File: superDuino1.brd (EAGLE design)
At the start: 70.8 x 71.1 mm, 25 parts

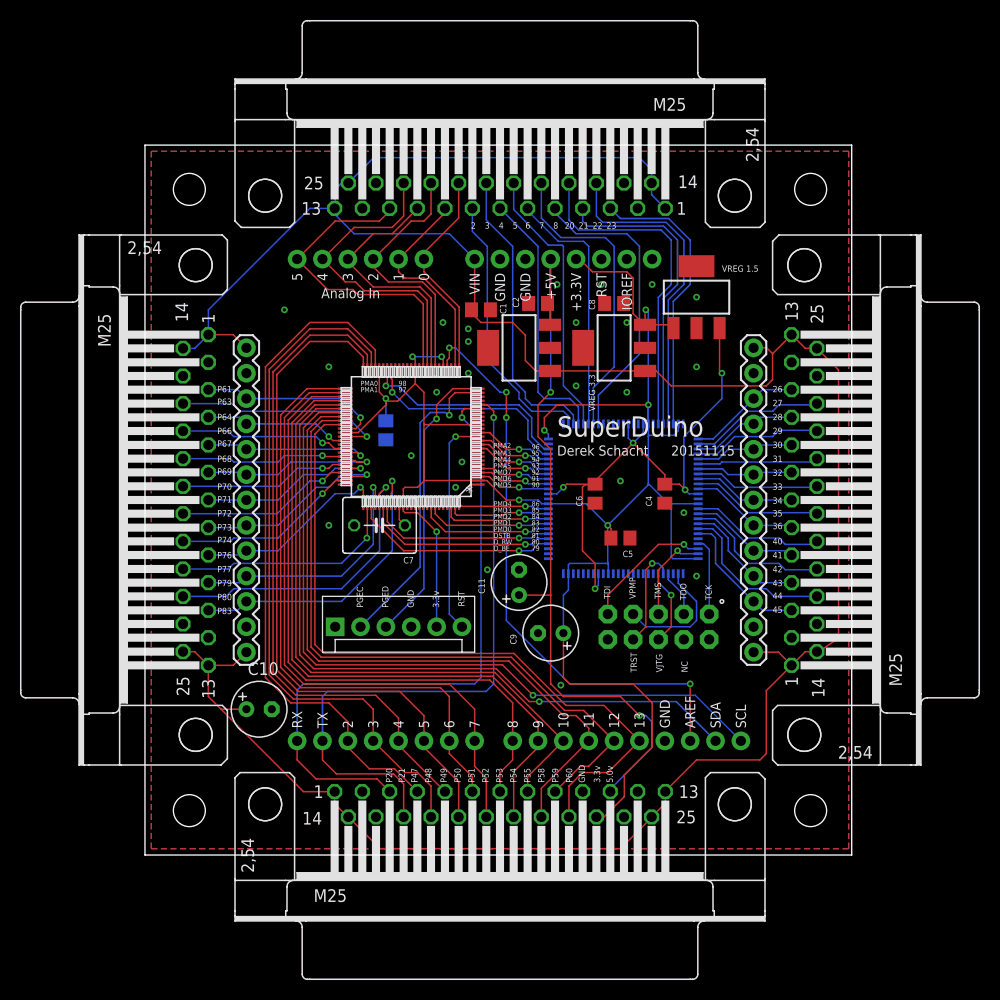
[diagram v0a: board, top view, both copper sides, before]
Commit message: Added a BOM file and updated schematic and layout to address: Issue #7, Issue #6, Issue #5, Issue #4, Issue #3, Issue #2, Issue #1
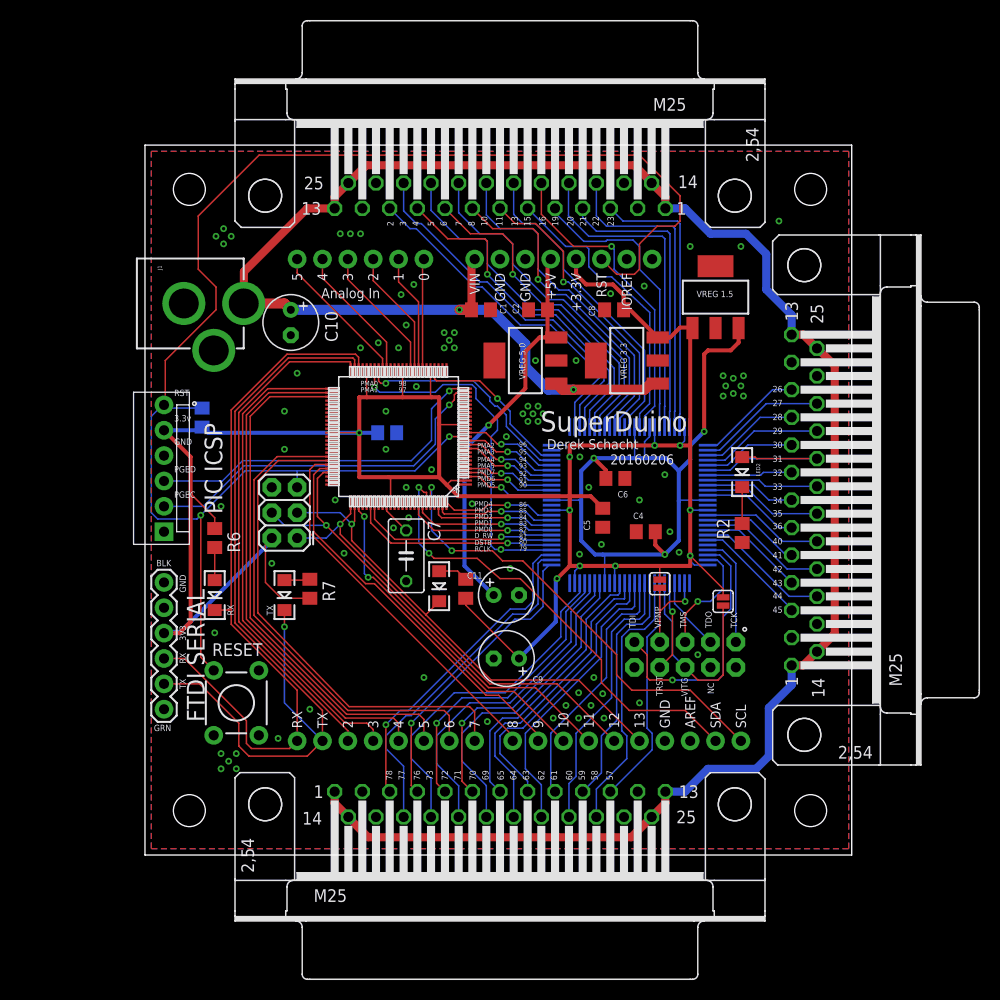
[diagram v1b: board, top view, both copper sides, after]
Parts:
- removed JP4: M13, SparkFun-Connectors:1X13
- removed X4: (no value), SparkFun-Connectors:M25H
- added J1: POWER_JACKPTH, SparkFun-Connectors:POWER_JACK_PTH
- added JP3: (no value), SparkFun-Connectors:1X06
- added LED1, LED2, RX, TX: (no value), SparkFun-LED:LED-1206
- added R1, R2, R3, R6, R7: (no value), rcl:R0805
- added R4, R5: SOLDERJUMPERNC, SparkFun-Retired:SJ_2S
- added S1: (no value), SparkFun-Electromechanical:TACTILE-PTH
- C7: value 10uF -> (none); device rcl:C050-055X075 -> rcl:C050-035X075
- JP2: value M13 -> (none); device SparkFun-Connectors:1X13 -> SparkFun-Connectors:2X3
- moved JP2 47.1 mm to (15.2, 31.8)
- moved C10 38.9 mm to (14.6, 53.3), turned to 270 degrees
- moved U$8 19.6 mm to (1.91, 32.4), turned to 90 degrees
- moved C9 5.12 mm to (36.2, 19.7)
- moved C4 4.26 mm to (50.2, 32.4), turned to 0 degrees
- moved C7 4.05 mm to (26.2, 30.0), turned to 270 degrees
- moved JP1 3.86 mm to (54.1, 20.1)
- moved C5 2.70 mm to (45.8, 33.8), turned to 90 degrees
- moved C6 2.54 mm to (47.1, 37.7), turned to 180 degrees
- moved U$6 1.91 mm to (57.1, 55.9)
- moved C11 1.80 mm to (36.2, 26.0), turned to 0 degrees
- moved U$5 1.80 mm to (48.3, 49.5)
- moved U$4 1.42 mm to (38.1, 49.5)
- moved U$1 1.27 mm to (25.4, 41.9)
- moved U$2 0.90 mm to (42.5, 42.5)
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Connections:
- net 1.5V renamed 1V5
- net DSTROBE renamed PMRW
- net N$10 renamed XA4
- net N$11 renamed XA16
- net N$12 renamed XA3
- net N$9 renamed XA17
- net RW renamed PMSTB
- net X2IO16 renamed XB16
- net X2IO17 renamed XB17
- net X2IO18 renamed XB18
- net X2IO19 renamed XB19
- net X2IO20 renamed XB20
- net X2IO22 renamed XB22
- net X2IO23 renamed XB23
- removed net 3.3V: C3.2, C5.2, C8.2, C9.+, U$1.16, U$1.2, U$1.30, U$1.37, U$1.46, U$1.62, U$1.86, U$2.100, U$2.18, U$2.24, U$2.39, U$2.50, U$2.66, U$2.74, U$2.87, U$3.3.3V, U$5.3, U$6.1, U$8.5, X3.23
- removed net 5V: C11.+, C2.1, U$3.5V, U$4.3, X3.11
- removed net AN0: U$1.26, U$3.A0, X1.21
- removed net AN1: U$1.27, U$3.A1, X1.9
- removed net AN2: U$1.32, U$3.A2, X1.22
- removed net AN3: U$1.33, U$3.A3, X1.10
- removed net AN4: U$1.34, U$3.A4, X1.23
- removed net AN5: U$1.35, U$3.A5, X1.11
- removed net AREF: U$1.29, U$3.AREF
- removed net BE: U$1.78, U$2.79
- removed net N$2 (its old number): U$2.2, X1.8
- removed net N$6: U$2.6, X1.6
- removed net N$7: U$2.7, X1.18
- removed net N$8: U$2.8, X1.5
- removed net PMA0: U$1.44, U$2.98
- removed net RAW: C1.1, C10.+, JP2.1, JP2.13, JP4.1, JP4.13, U$3.VIN, U$4.1, U$5.1, X1.1, X1.13, X1.14, X1.25, X2.1, X2.13, X2.14, X2.25, X3.1, X3.13, X3.14, X3.25, X4.1, X4.13, X4.14, X4.25
- removed net X2IO10: JP2.10, U$2.28, X2.10
- removed net X2IO11: JP2.11, U$2.26, X2.11
- removed net X2IO21: U$2.31, X2.21
- removed net X2IO3: JP2.3, U$2.45, X2.3
- removed net X2IO4: JP2.4, U$2.43, X2.4
- removed net X2IO5: JP2.5, U$2.41, X2.5
- removed net X2IO6: JP2.6, U$2.36, X2.6
- removed net X2IO7: JP2.7, U$2.34, X2.7
- removed net X2IO8: JP2.8, U$2.32, X2.8
- removed net X2IO9: JP2.9, U$2.30, X2.9
- removed net X4IO10: JP4.10, U$1.79, X4.10
- removed net X4IO11: JP4.11, U$1.83, X4.11
- removed net X4IO16: U$1.63, X4.16
- removed net X4IO17: U$1.66, X4.17
- removed net X4IO18: U$1.68, X4.18
- removed net X4IO19: U$1.70, X4.19
- removed net X4IO20: U$1.72, X4.20
- removed net X4IO21: U$1.74, X4.21
- removed net X4IO22: U$1.77, X4.22
- removed net X4IO23: U$1.80, X4.23
- removed net X4IO3: JP4.3, U$1.61, X4.3
- removed net X4IO4: JP4.4, U$1.64, X4.4
- removed net X4IO5: JP4.5, U$1.67, X4.5
- removed net X4IO6: JP4.6, U$1.69, X4.6
- removed net X4IO7: JP4.7, U$1.71, X4.7
- removed net X4IO8: JP4.8, U$1.73, X4.8
- removed net X4IO9: JP4.9, U$1.76, X4.9
- new net 3V3: C3.2, C5.2, C8.2, C9.+, JP2.2, JP3.VCC, R1.1, R3.1, R4.2, R5.2, R6.1, R7.1, U$1.16, U$1.2, U$1.30, U$1.37, U$1.46, U$1.62, U$1.86, U$2.100, U$2.18, U$2.24, U$2.39, U$2.50, U$2.66, U$2.74, U$2.87, U$3.3.3V, U$5.3, U$6.1, U$8.5
- new net 5V0: C11.+, C2.1, U$3.5V, U$4.3
- new net A0: U$1.32, U$3.A0
- new net A1: U$1.33, U$3.A1
- new net A2: U$1.34, U$3.A2
- new net A3: U$1.35, U$3.A3
- new net A4: U$1.41, U$3.A4
- new net A5: U$1.42, U$3.A5
- new net N$1: LED1.A, R1.2
- new net PMA6: U$1.29, U$2.98
- new net REFO: U$1.44, U$2.79
- new net VRAW: C1.1, C10.+, J1.PWR, U$3.VIN, U$4.1, U$5.1, X1.1, X1.13, X1.14, X1.25, X2.1, X2.13, X2.14, X2.25, X3.1, X3.13, X3.14, X3.25
- new net XA10: U$2.4, X1.10
- new net XA11: U$2.2, X1.11
- new net XA18: U$2.16, X1.18
- new net XA19: U$2.13, X1.19
- new net XA20: U$2.10, X1.20
- new net XA21: U$2.7, X1.21
- new net XA22: U$2.5, X1.22
- new net XA23: U$2.3, X1.23
- new net XA5: U$2.19, X1.5
- new net XA6: U$2.15, X1.6
- new net XA7: U$2.11, X1.7
- new net XA8: U$2.8, X1.8
- new net XA9: U$2.6, X1.9
- new net XB10: U$2.28, X2.10
- new net XB11: U$2.26, X2.11
- new net XB21: LED2.A, U$2.31, X2.21
- new net XB3: U$2.45, X2.3
- new net XB4: U$2.43, X2.4
- new net XB5: U$2.41, X2.5
- new net XB6: U$2.36, X2.6
- new net XB7: U$2.34, X2.7
- new net XB8: U$2.32, X2.8
- new net XB9: U$2.30, X2.9
- new net XC10: U$2.59, X3.10
- new net XC11: U$2.57, X3.11
- new net XC16: U$2.77, X3.16
- new net XC17: U$2.73, X3.17
- new net XC18: U$2.71, X3.18
- new net XC19: U$2.69, X3.19
- new net XC20: U$2.64, X3.20
- new net XC21: U$2.62, X3.21
- new net XC22: U$2.60, X3.22
- new net XC23: U$2.58, X3.23
- new net XC3: U$2.78, X3.3
- new net XC4: U$2.76, X3.4
- new net XC5: U$2.72, X3.5
- new net XC6: U$2.70, X3.6
- new net XC7: U$2.65, X3.7
- new net XC8: U$2.63, X3.8
- new net XC9: U$2.61, X3.9
- net D10: now also U$1.78; no longer U$1.55, X3.8
- net D11: now also JP2.4, U$1.72; no longer U$1.58, X3.21
- net D12: now also JP2.1, U$1.76; no longer U$1.59, X3.9
- net D13: now also JP2.3, LED1.C, U$1.77; no longer U$1.60, X3.22
- net D2: now also U$1.50; no longer U$1.47, X3.4
- net D3: now also U$1.51; no longer U$1.48, X3.17
- net D4: now also U$1.52; no longer U$1.49, X3.5
- net D5: now also U$1.53; no longer U$1.50, X3.18
- net D6: now also U$1.68; no longer U$1.51, X3.6
- net D7: now also U$1.69; no longer U$1.52, X3.19
- net D8: now also U$1.70; no longer U$1.53, X3.7
- net D9: now also U$1.71; no longer U$1.54, X3.20
- net GND: now also J1.GND, J1.GNDBREAK, JP2.6, JP3.GND, R2.1, S1.1; no longer JP2.12, JP2.2, JP4.12, JP4.2, U$1.28, X3.10, X4.12, X4.15, X4.2, X4.24
- net N$3: now also LED2.C, R2.2; no longer U$2.3, X1.20
- net N$4: now also R7.2, TX.A; no longer U$2.4, X1.7
- net N$5: now also R6.2, RX.A; no longer U$2.5, X1.19
- net RST: now also JP2.5, R3.2, S1.3, U$3.RES
- net RX: now also JP3.TXO, RX.C, U$1.48; no longer U$1.20, X3.3
- net SCL: now also U$1.96; no longer U$1.57
- net SDA: now also U$1.95; no longer U$1.56
- net TX: now also JP3.RXI, TX.C, U$1.49; no longer U$1.21, X3.16
- net VJTAG: now also R5.1
- net VPUMP: now also R4.1
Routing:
- net RAW: track 265.6 -> 0.00 mm
- net 3V3: track 0.00 -> 262.9 mm, vias 0 -> 10
- net VRAW: track 0.00 -> 227.5 mm, vias 0 -> 2
- net 3.3V: track 196.6 -> 0.00 mm, vias 9 -> 0
- net RST: track 22.0 -> 157.2 mm, vias 1 -> 2
- net 5V: track 74.1 -> 0.00 mm, vias 2 -> 0
- net AREF: track 59.5 -> 0.00 mm, vias 4 -> 0
- net 5V0: track 0.00 -> 39.9 mm, vias 0 -> 1
- net XA23: track 0.00 -> 36.1 mm
- net XA22: track 0.00 -> 36.0 mm
- net REFO: track 0.00 -> 35.7 mm, vias 0 -> 2
- net XC16: track 0.00 -> 35.1 mm
- net XA10: track 0.00 -> 34.6 mm, vias 0 -> 1
- net XA21: track 0.00 -> 34.6 mm
- net XC17: track 0.00 -> 34.2 mm
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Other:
- board text added: "10"
- board text added: "11"
- board text added: "13"
- board text added: "15"
- board text added: "16"
- board text added: "19"
- board text added: "20160206"
- board text added: "3V3"
- board text added: "57"
- board text added: "58"
- board text added: "59"
- board text added: "60"
- board text added: "61"
- board text added: "62"
- board text added: "63"
- board text added: "64"
- board text added: "65"
- board text added: "69"
- board text added: "70"
- board text added: "71"
- board text added: "72"
- board text added: "73"
- board text added: "76"
- board text added: "77"
- board text added: "78"
- board text added: "BLK"
- board text added: "FTDI SERIAL"
- board text added: "GRN"
- board text added: "PIC ICSP"
- board text added: "RCLK"
- board text added: "RESET"
- board text added: "RX"
- board text added: "TX"
- board text added: "VREG 5.0"
- board text removed: "20151115"
- board text removed: "5.0v"
- board text removed: "D_BE"
- board text removed: "P20"
- board text removed: "P21"
- board text removed: "P47"
- board text removed: "P48"
- board text removed: "P49"
- board text removed: "P50"
- board text removed: "P51"
- board text removed: "P52"
- board text removed: "P53"
- board text removed: "P54"
- board text removed: "P55"
- board text removed: "P58"
- board text removed: "P59"
- board text removed: "P60"
- board text removed: "P61"
- board text removed: "P63"
- board text removed: "P64"
- board text removed: "P66"
- board text removed: "P67"
- board text removed: "P68"
- board text removed: "P69"
- board text removed: "P70"
- board text removed: "P71"
- board text removed: "P72"
- board text removed: "P73"
- board text removed: "P74"
- board text removed: "P76"
- board text removed: "P77"
- board text removed: "P79"
- board text removed: "P80"
- board text removed: "P83"
